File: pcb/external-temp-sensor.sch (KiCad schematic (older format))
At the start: 13 parts, among them P1 TEMP, P2 SERIAL, P3 PWR, SW1 RESET, SW2 FLASH, U1 ESP-12F, U2 OKI-78SR

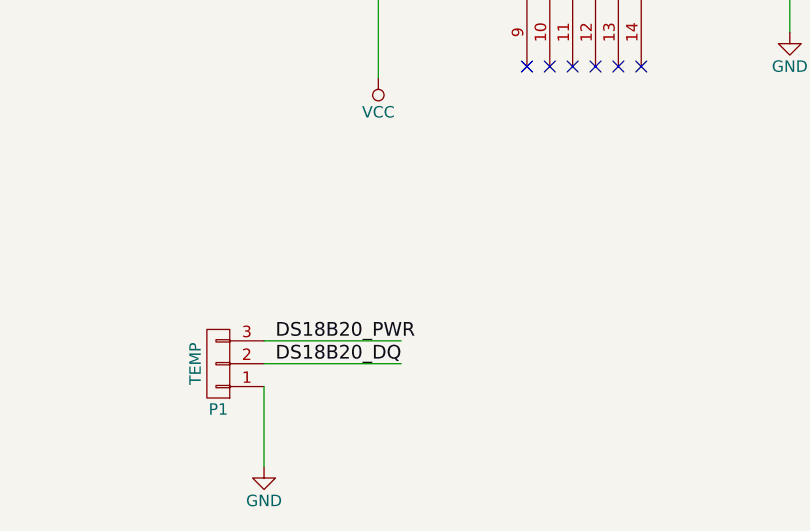
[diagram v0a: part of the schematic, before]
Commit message: Add pull-up resistor
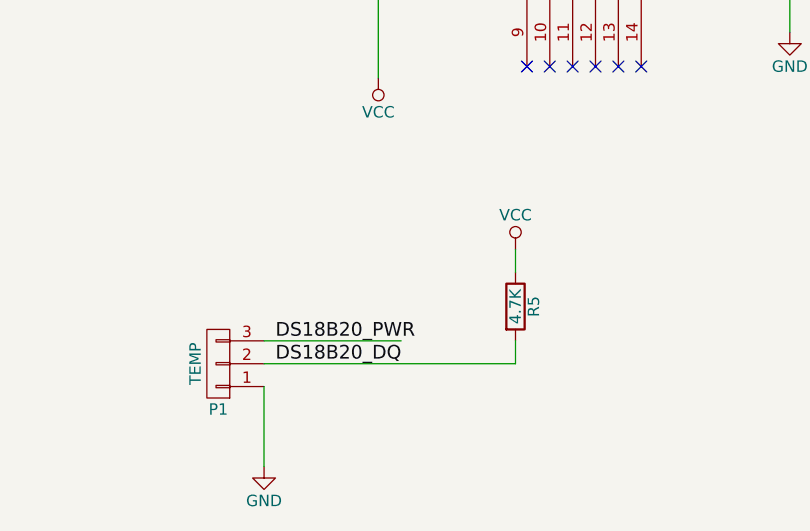
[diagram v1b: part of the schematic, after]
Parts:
- added R5: 4.7K, Resistors_SMD:R_1206_HandSoldering, symbol R
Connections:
- wire segments 38 -> 40
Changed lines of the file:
@@
 DS18B20_DQ
 Wire Wire Line
-	4450 5500 5050 5500
+	4450 5500 5550 5500
 Wire Wire Line
 	4450 5400 5050 5400
@@
 Text Label 4400 3000 0    60   ~ 0
 RESET
+$Comp
+L VCC #PWR014
+U 1 1 58AF4E2E
+P 5550 5000
+F 0 "#PWR014" H 5550 4850 50  0001 C CNN
+F 1 "VCC" H 5550 5150 50  0000 C CNN
+F 2 "" H 5550 5000 50  0000 C CNN
+F 3 "" H 5550 5000 50  0000 C CNN
+	1    5550 5000
+	1    0    0    -1
+$EndComp
+$Comp
+L R R5
+U 1 1 58AF4E60
+P 5550 5250
+F 0 "R5" V 5630 5250 50  0000 C CNN
+F 1 "4.7K" V 5550 5250 50  0000 C CNN
+F 2 "Resistors_SMD:R_1206_HandSoldering" V 5480 5250 50  0001 C CNN
+F 3 "" H 5550 5250 50  0000 C CNN
+	1    5550 5250
+	1    0    0    -1
+$EndComp
+Wire Wire Line
+	5550 5000 5550 5100
+Wire Wire Line
+	5550 5500 5550 5400
 $EndSCHEMATC
